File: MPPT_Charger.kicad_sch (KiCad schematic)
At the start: 113 parts, among them J1 Solar, J2 Battery, J3 USB_B_Mini, J4 INTERFACE PORT, J6 JTAG, J8 Micro_SD_Card_Det_Hirose_DM3AT, J9 IIC RTC, Q1 CSD19505KCS, Q11 CSD19505KCS, Q12 CSD19505KCS, Q13 CSD19505KCS, Q2 CSD19505KCS, Q3 CSD19505KCS, Q4 Si2306, Q5 MMBT3904 1A, Q6 MMBT3904 1A, Q7 Si2306, U1 ACS712, U10 ADS1015, U2 B1212S, U3 AMS1117-5.0, U4 AMS1117-3.3, U5 XL7005A, U6 XL7005A, U7 IR2104, U8 ESP32, U9 CH340G

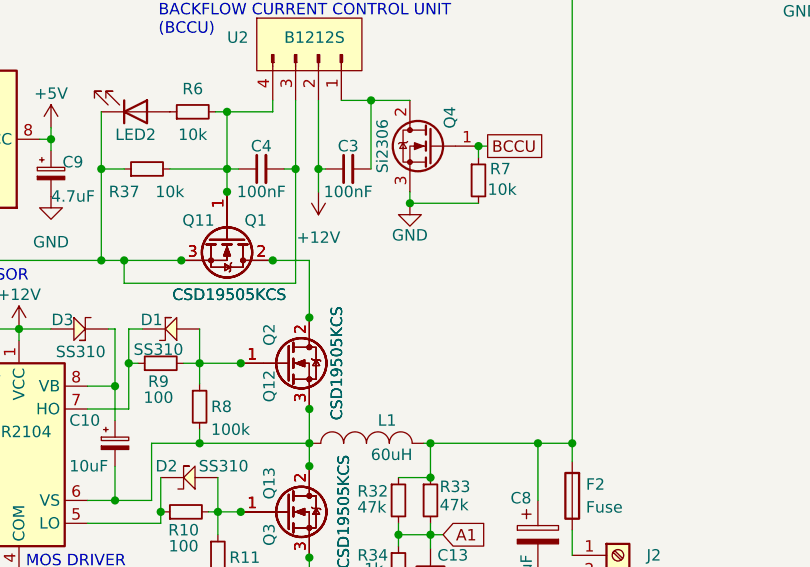
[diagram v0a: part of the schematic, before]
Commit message: Heatsink and insulation ToDo: Smaller heatsink
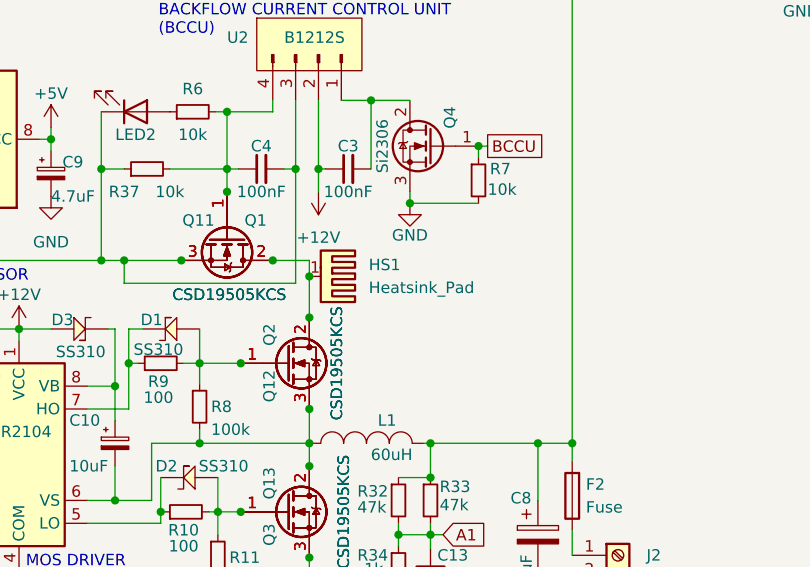
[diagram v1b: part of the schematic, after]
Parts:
- added HS1: Heatsink_Pad, Heatsink:Heatsink_125x35x50mm_3xFixationM3, symbol Mechanical:Heatsink_Pad
- Q13, Q3: footprint Package_TO_SOT_THT:TO-220-3_Vertical -> Library:TO-220-3_Vertical_Insulated
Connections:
- net at Q1.2 (D), Q11.2 (D), Q12.2 (D)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: now also HS1.1
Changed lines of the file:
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@@
   (junction (at 261.62 133.604) (diameter 0) (color 0 0 0 0)
   )
+  (junction (at 87.376 101.6) (diameter 0) (color 0 0 0 0)
+  )
   (junction (at 257.048 110.998) (diameter 0) (color 0 0 0 0)
   )
@@
     (stroke (width 0) (type default) (color 0 0 0 0))
   )
+  (wire (pts (xy 87.376 101.6) (xy 87.376 99.822))
+    (stroke (width 0) (type default) (color 0 0 0 0))
+  )
   (wire (pts (xy 33.528 149.606) (xy 37.084 149.606))
     (stroke (width 0) (type default) (color 0 0 0 0))
@@
     (stroke (width 0) (type default) (color 0 0 0 0))
   )
-  (wire (pts (xy 87.376 106.172) (xy 87.376 99.822))
+  (wire (pts (xy 87.376 106.172) (xy 87.376 101.6))
     (stroke (width 0) (type default) (color 0 0 0 0))
   )
@@
     (pin "3")
   )
+  (symbol (lib_id "Mechanical:Heatsink_Pad") (at 89.916 101.6 270) (unit 1)
+    (in_bom yes) (on_board yes) (fields_autoplaced)
+    (property "Reference" "HS1" (id 0) (at 93.98 100.3172 90)
+      (effects (font (size 1.27 1.27)) (justify left))
+    )
+    (property "Value" "Heatsink_Pad" (id 1) (at 93.98 102.8572 90)
+      (effects (font (size 1.27 1.27)) (justify left))
+    )
+    (property "Footprint" "Heatsink:Heatsink_125x35x50mm_3xFixationM3" (id 2) (at 88.646 101.9048 0)
+      (effects (font (size 1.27 1.27)) hide)
+    )
+    (property "Datasheet" "~" (id 3) (at 88.646 101.9048 0)
+      (effects (font (size 1.27 1.27)) hide)
+    )
+    (pin "1")
+  )
   (symbol (lib_id "Device:R_Small") (at 43.434 132.842 0) (unit 1)
     (in_bom yes) (on_board yes)
@@
     (property "Reference" "Q3" (id 0) (at 82.931 130.302 90))
     (property "Value" "CSD19505KCS" (id 1) (at 91.186 127.762 90))
-    (property "Footprint" "Package_TO_SOT_THT:TO-220-3_Vertical" (id 2) (at 93.218 142.748 90)
+    (property "Footprint" "Library:TO-220-3_Vertical_Insulated" (id 2) (at 93.218 142.748 90)
       (effects (font (size 1.27 1.27) italic) (justify left) hide)
     )
@@
     (property "Reference" "Q13" (id 0) (at 82.931 124.587 90))
     (property "Value" "CSD19505KCS" (id 1) (at 91.186 127.762 90))
-    (property "Footprint" "Package_TO_SOT_THT:TO-220-3_Vertical" (id 2) (at 93.218 142.748 90)
+    (property "Footprint" "Library:TO-220-3_Vertical_Insulated" (id 2) (at 93.218 142.748 90)
       (effects (font (size 1.27 1.27) italic) (justify left) hide)
     )
@@
       (reference "F2") (unit 1) (value "Fuse") (footprint "Fuse:Fuse_Blade_ATO_directSolder")
     )
+    (path "/06f39674-a969-4ef5-9af7-a5fbc220e67c"
+      (reference "HS1") (unit 1) (value "Heatsink_Pad") (footprint "Heatsink:Heatsink_125x35x50mm_3xFixationM3")
+    )
     (path "/b468fa50-d53d-4dd2-b004-16844579a7be"
       (reference "J1") (unit 1) (value "Solar") (footprint "footprints:TerminalBlock_DEGSON_DG135T")
@@
     )
     (path "/bb113282-5d8f-4b0b-a4b8-2446b034aad5"
-      (reference "Q3") (unit 1) (value "CSD19505KCS") (footprint "Package_TO_SOT_THT:TO-220-3_Vertical")
+      (reference "Q3") (unit 1) (value "CSD19505KCS") (footprint "Library:TO-220-3_Vertical_Insulated")
     )
     (path "/d518002e-8259-4f21-880a-acde968c86e4"
@@
     )
     (path "/dd65f54c-87a0-4385-98b4-810c8b6410c7"
-      (reference "Q13") (unit 1) (value "CSD19505KCS") (footprint "Package_TO_SOT_THT:TO-220-3_Vertical")
+      (reference "Q13") (unit 1) (value "CSD19505KCS") (footprint "Library:TO-220-3_Vertical_Insulated")
     )
     (path "/c953cab7-4946-4acc-9567-3e799c6ea44c"

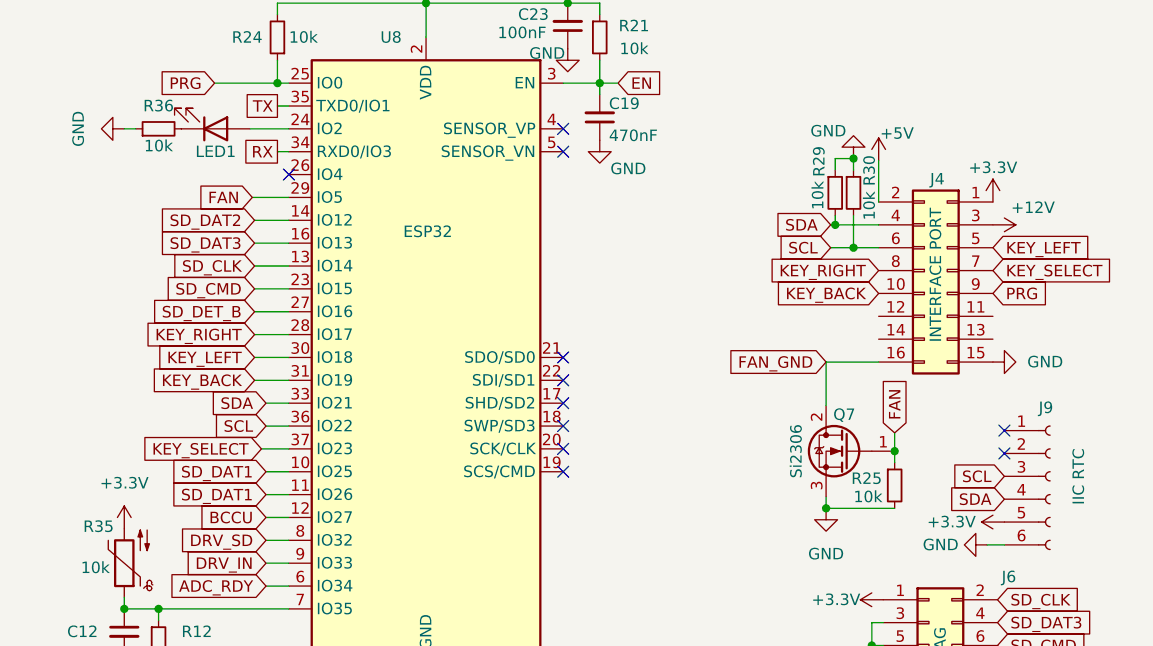
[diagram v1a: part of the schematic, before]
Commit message: Footprint C+R changed to 0603 where possible
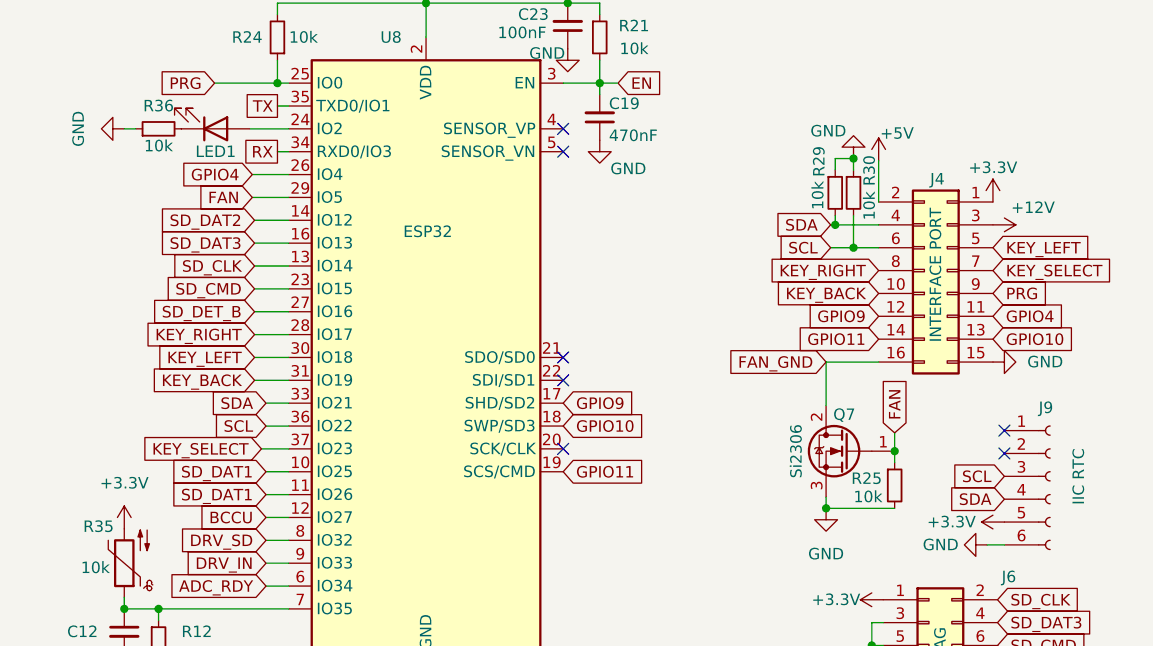
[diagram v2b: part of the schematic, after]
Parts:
- C21, C22, C5, C6, C9: footprint Capacitor_SMD:C_0805_2012Metric -> Capacitor_SMD:C_0603_1608Metric
- R1, R10, R11, R12, R13, R14, R15, R16, R17, R18, R19, R2, R20, R21, R22, R23, R24, R25, R26, R27, R28, R29, R3, R30, R31, R32, R33, R34, R36, R37, R38, R39, R4, R40, R5, R6, R7, R8, R9: footprint Resistor_SMD:R_0805_2012Metric -> Resistor_SMD:R_0603_1608Metric
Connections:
- net GPIO4: now reaches J4.11 (Pin_11)
- net GPIO4: now also U8.26 (IO4)
- net GPIO9: now reaches J4.12 (Pin_12)
- net GPIO9: now also U8.17 (SHD/SD2)
- net GPIO10: now reaches J4.13 (Pin_13)
- net GPIO10: now also U8.18 (SWP/SD3)
- net GPIO11: now reaches J4.14 (Pin_14)
- net GPIO11: now also U8.19 (SCS/CMD)
- no-connect marks 21 -> 17

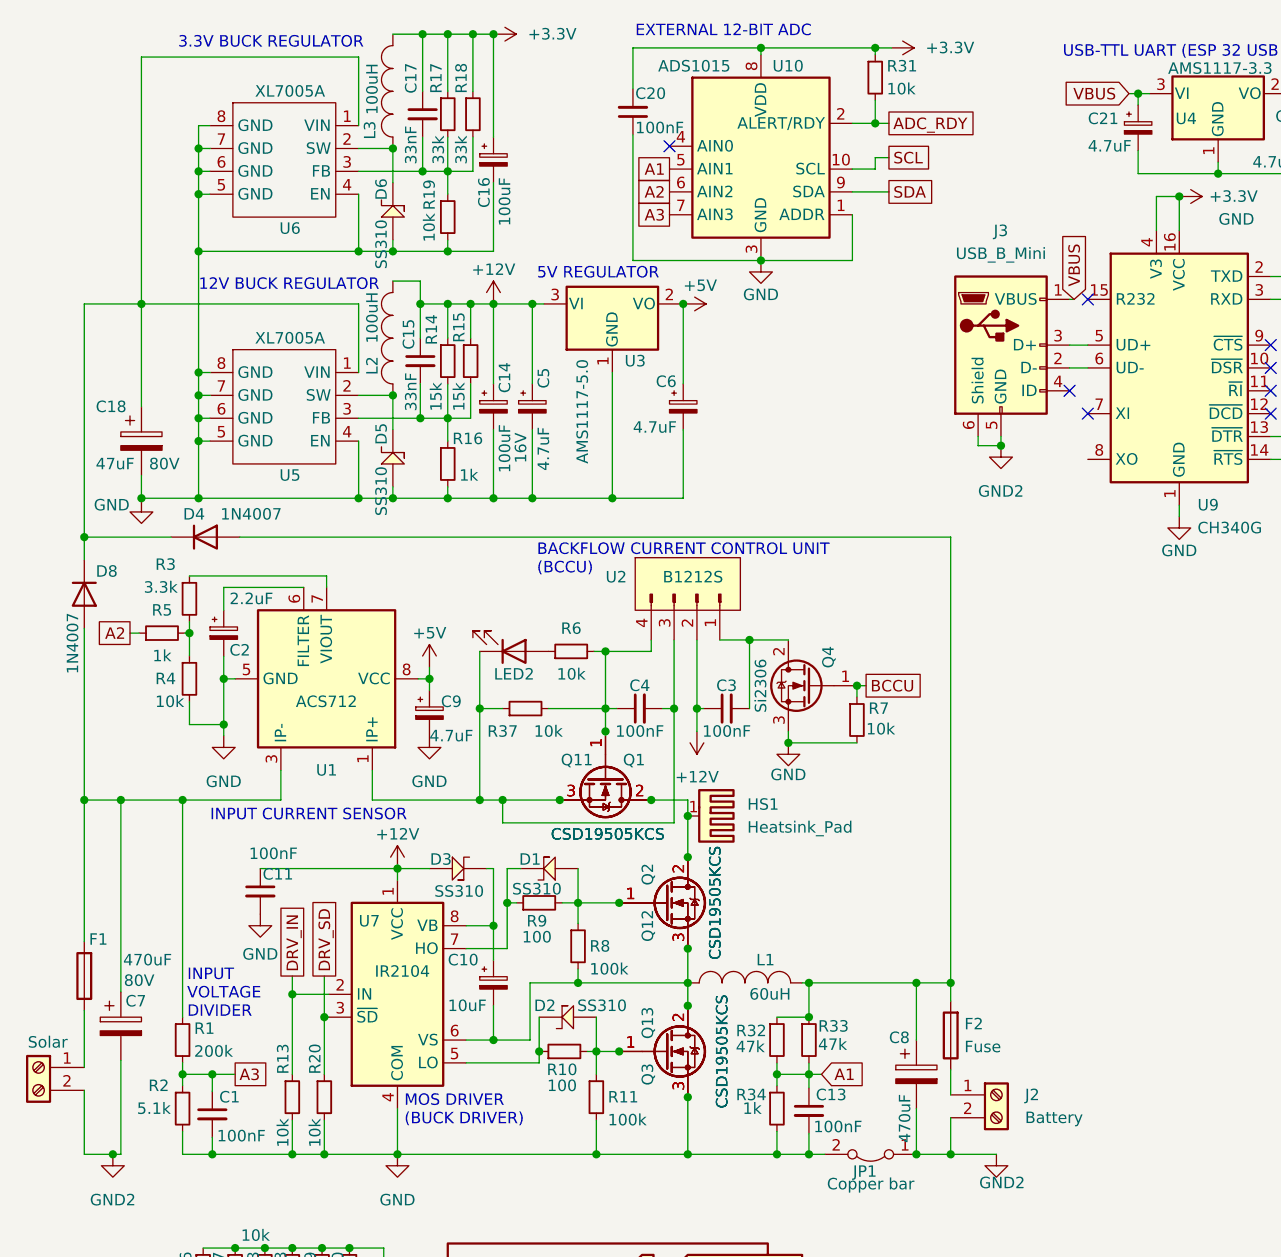
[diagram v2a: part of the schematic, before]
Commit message: Footprint updates for some parts (mainly too small drill holes for screw terminal and larger capacitors)
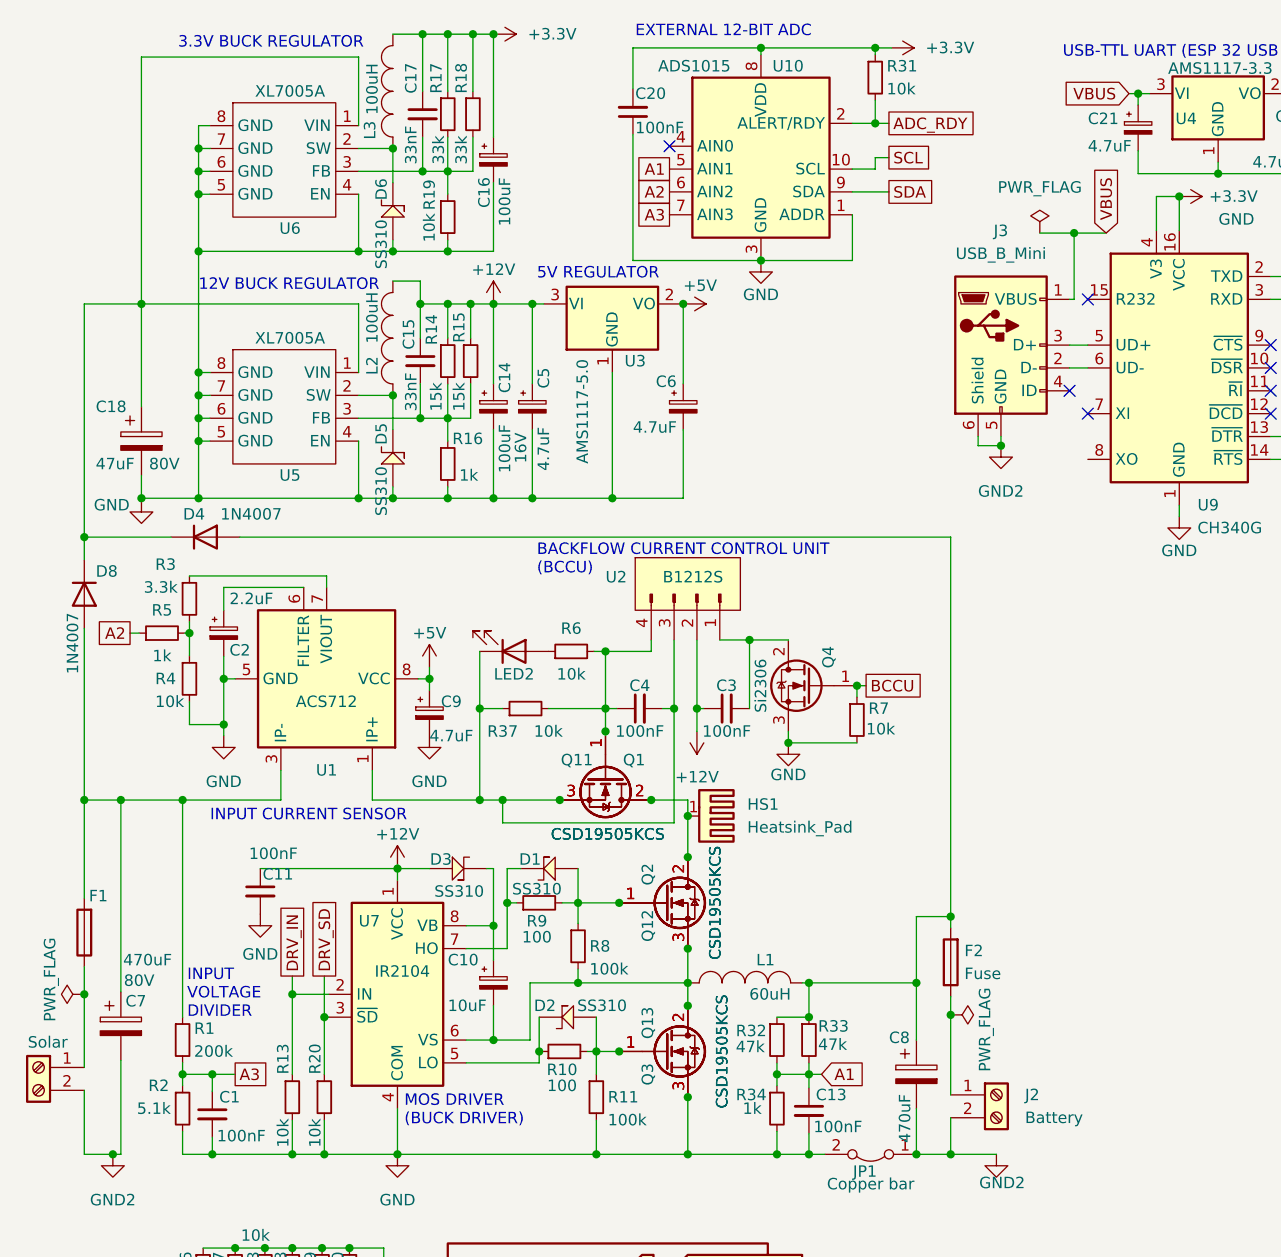
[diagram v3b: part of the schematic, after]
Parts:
- J1, J2: footprint footprints:TerminalBlock_DEGSON_DG135T -> Library:TerminalBlock_DEGSON_DG135T
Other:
- moved on the sheet: F1, F2

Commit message: Footprint for 470uF was too small Some more minor changes
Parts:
- C7, C8: footprint Capacitor_THT:C_Radial_D12.5mm_H20.0mm_P5.00mm -> Capacitor_THT:CP_Radial_D16.0mm_P7.50mm
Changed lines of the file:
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@@
       (effects (font (size 1.27 1.27)) (justify left))
     )
-    (property "Footprint" "Capacitor_THT:C_Radial_D12.5mm_H20.0mm_P5.00mm" (id 2) (at 113.7412 134.112 0)
+    (property "Footprint" "Capacitor_THT:CP_Radial_D16.0mm_P7.50mm" (id 2) (at 113.7412 134.112 0)
       (effects (font (size 1.27 1.27)) hide)
     )
@@
       (effects (font (size 1.27 1.27)) (justify left))
     )
-    (property "Footprint" "Capacitor_THT:C_Radial_D12.5mm_H20.0mm_P5.00mm" (id 2) (at 25.3492 128.778 0)
+    (property "Footprint" "Capacitor_THT:CP_Radial_D16.0mm_P7.50mm" (id 2) (at 25.3492 128.778 0)
       (effects (font (size 1.27 1.27)) hide)
     )
@@
     )
     (path "/159a177d-5e2f-470e-949c-7f78e34a2af3"
-      (reference "C7") (unit 1) (value "470uF") (footprint "Capacitor_THT:C_Radial_D12.5mm_H20.0mm_P5.00mm")
+      (reference "C7") (unit 1) (value "470uF") (footprint "Capacitor_THT:CP_Radial_D16.0mm_P7.50mm")
     )
     (path "/010c0f5e-e63a-4a17-9c19-17f7a9a1e6e0"
-      (reference "C8") (unit 1) (value "470uF") (footprint "Capacitor_THT:C_Radial_D12.5mm_H20.0mm_P5.00mm")
+      (reference "C8") (unit 1) (value "470uF") (footprint "Capacitor_THT:CP_Radial_D16.0mm_P7.50mm")
     )
     (path "/d1824afa-7dff-48a7-8516-96dbd7898808"
